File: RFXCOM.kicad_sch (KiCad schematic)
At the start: 23 parts, among them J1 TX Antenna, J2 RX Antenna, J3 SWD_Connector, J4 Rx, J5 Tx, J7 SWD, U1 STM32L412KBTx, Y1 16M

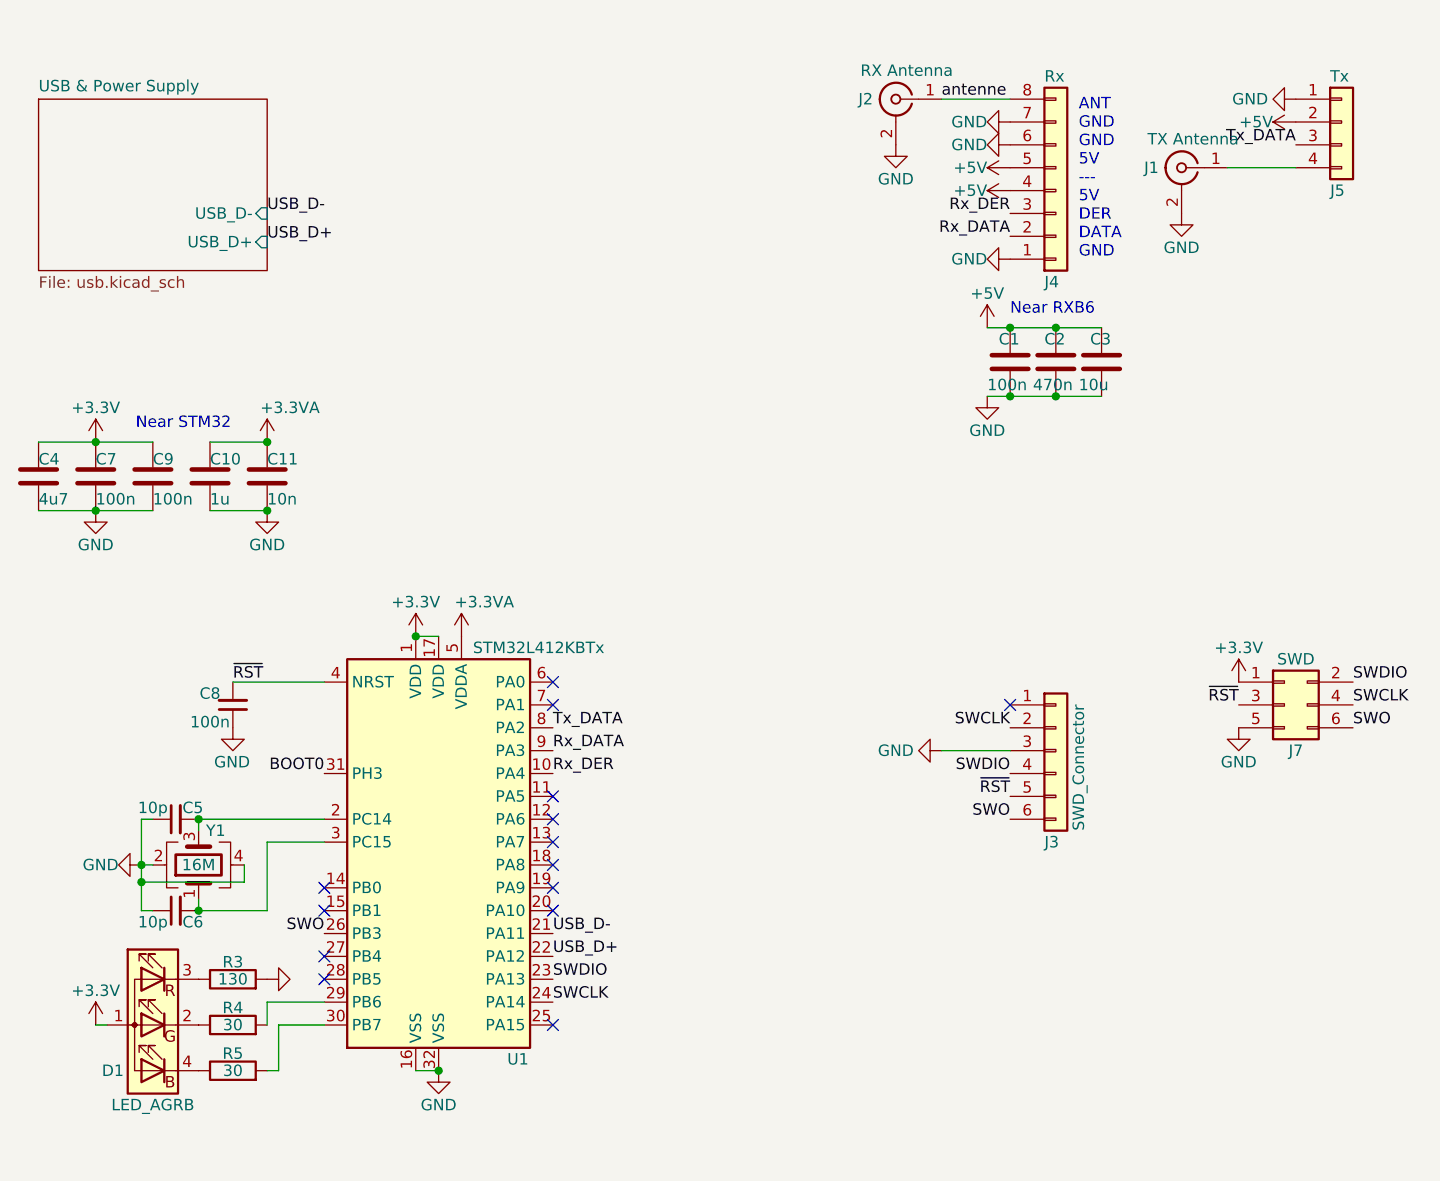
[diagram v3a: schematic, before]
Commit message: add cc110L
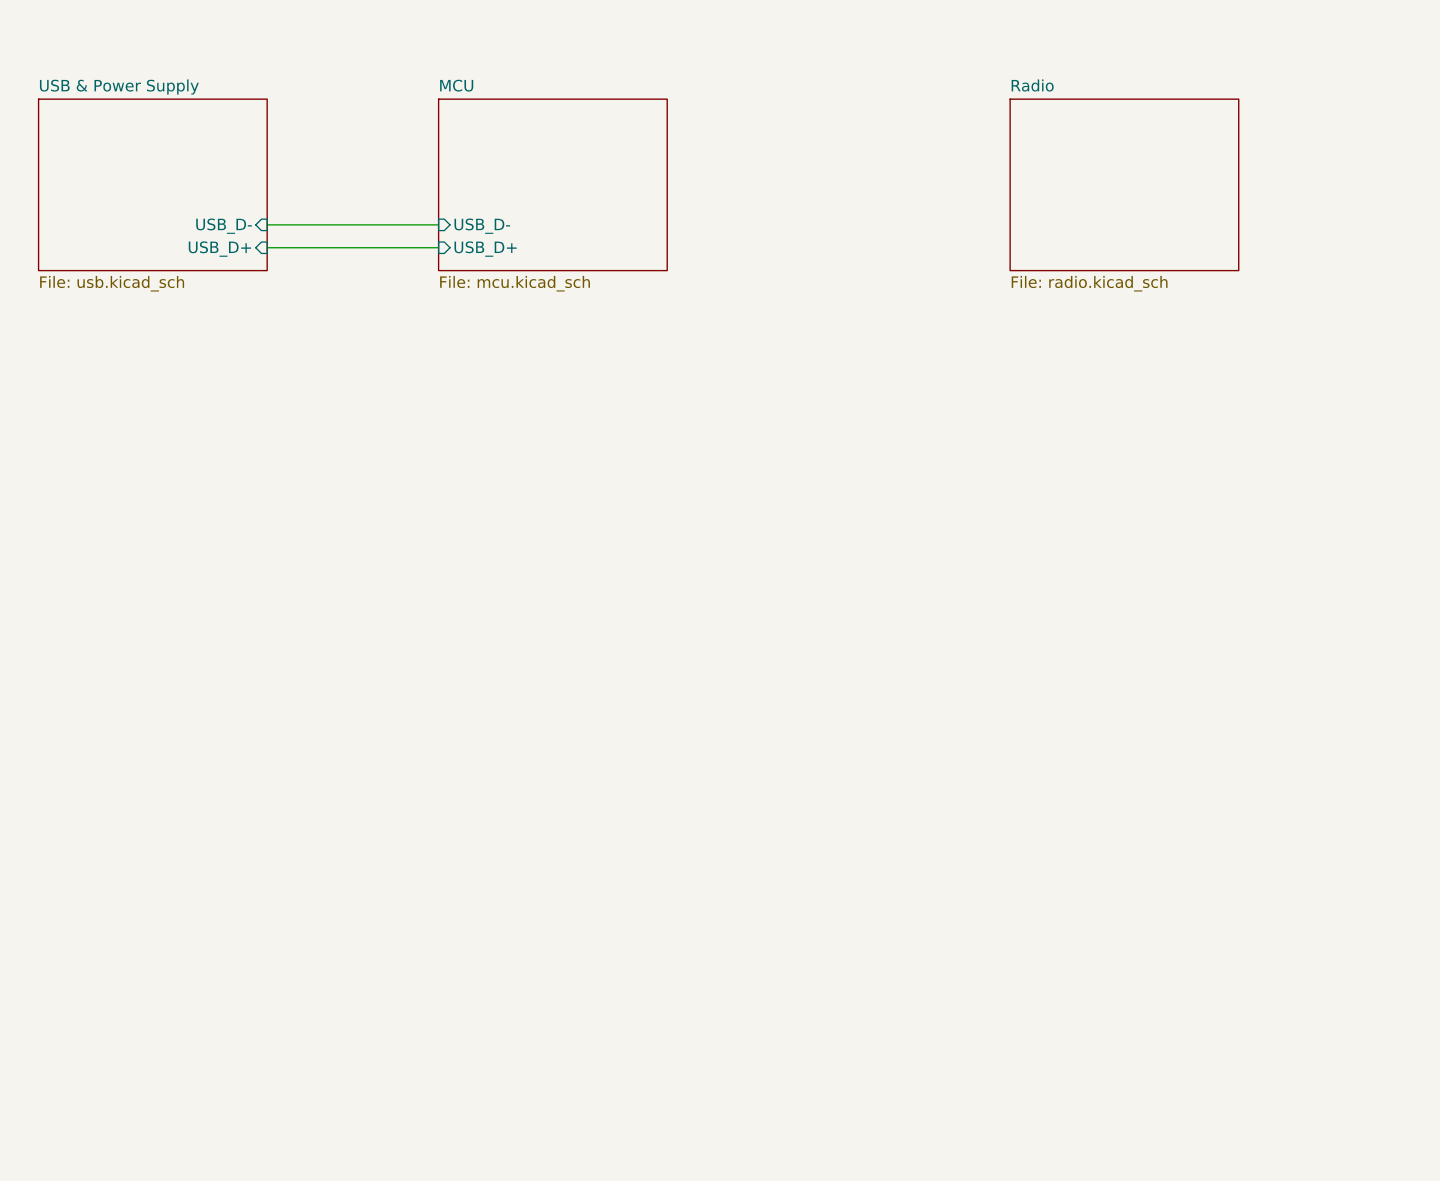
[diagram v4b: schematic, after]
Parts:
- removed C1: 100n, Capacitor_SMD:C_0805_2012Metric_Pad1.18x1.45mm_HandSolder, symbol Device:C
- removed C10: 1u, Capacitor_SMD:C_0603_1608Metric_Pad1.08x0.95mm_HandSolder, symbol Device:C
- removed C11: 10n, Capacitor_SMD:C_0603_1608Metric_Pad1.08x0.95mm_HandSolder, symbol Device:C
- removed C2: 470n, Capacitor_SMD:C_0805_2012Metric_Pad1.18x1.45mm_HandSolder, symbol Device:C
- removed C3: 10u, Capacitor_SMD:C_0805_2012Metric_Pad1.18x1.45mm_HandSolder, symbol Device:C
- removed C4: 4u7, Capacitor_SMD:C_0805_2012Metric_Pad1.18x1.45mm_HandSolder, symbol Device:C
- removed C5, C6: 10p, Capacitor_SMD:C_0603_1608Metric_Pad1.08x0.95mm_HandSolder, symbol Device:C_Small
- removed C7, C9: 100n, Capacitor_SMD:C_0603_1608Metric_Pad1.08x0.95mm_HandSolder, symbol Device:C
- removed C8: 100n, Capacitor_SMD:C_0603_1608Metric_Pad1.08x0.95mm_HandSolder, symbol Device:C_Small
- removed D1: LED_AGRB, LED_SMD:LED_RGB_Wuerth-PLCC4_3.2x2.8mm_150141M173100, symbol Device:LED_AGRB
- removed J1: TX Antenna, Connector_Coaxial:SMA_Amphenol_901-144_Vertical, symbol Connector:Conn_Coaxial
- removed J2: RX Antenna, Connector_Coaxial:SMA_Amphenol_901-144_Vertical, symbol Connector:Conn_Coaxial
- removed J3: SWD_Connector, Connector_PinHeader_2.54mm:PinHeader_1x06_P2.54mm_Vertical, symbol Connector_Generic:Conn_01x06
- removed J4: Rx, rf_components:RXB6, symbol Connector_Generic:Conn_01x08
- removed J5: Tx, rf_components:XKFST_Horizontal, symbol Connector_Generic:Conn_01x04
- removed J7: SWD, Connector_PinHeader_1.27mm:PinHeader_2x03_P1.27mm_Vertical_SMD, symbol Connector_Generic:Conn_02x03_Odd_Even
- removed R3: 130, Resistor_SMD:R_0805_2012Metric_Pad1.20x1.40mm_HandSolder, symbol Device:R
- removed R4, R5: 30, Resistor_SMD:R_0805_2012Metric_Pad1.20x1.40mm_HandSolder, symbol Device:R
- removed U1: STM32L412KBTx, Package_DFN_QFN:QFN-32-1EP_5x5mm_P0.5mm_EP3.45x3.45mm, symbol stm32l412:STM32L412KBTx
- removed Y1: 16M, Crystal:Crystal_SMD_Abracon_ABM8G-4Pin_3.2x2.5mm, symbol Device:Crystal_GND24
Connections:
- no-connect marks 14 -> 0
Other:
- added sheet MCU (mcu.kicad_sch)
- added sheet Radio (radio.kicad_sch)
- note removed: "ANT GND GND 5V --- 5V DER DATA GND"
- note removed: "Near RXB6"
- note removed: "Near STM32"
